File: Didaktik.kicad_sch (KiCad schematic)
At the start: 102 parts, among them J1 Conn_01x04_MountingPin, SW1 SW_Push, SW10 SW_Push_45deg, SW11 SW_Push_45deg, SW12 SW_Push_45deg, SW13 SW_Push_45deg, SW14 SW_Push_45deg, SW15 SW_Push_45deg, SW16 SW_Push_45deg, SW17 SW_Push_45deg, SW18 SW_Push_45deg, SW19 SW_Push_45deg, SW2 SW_Push_45deg, SW20 SW_Push_45deg, SW21 SW_Push_45deg, SW22 SW_Push_45deg, SW23 SW_Push_45deg, SW24 SW_Push_45deg, SW25 SW_Push_45deg, SW26 SW_Push_45deg, SW27 SW_Push_45deg, SW28 SW_Push_45deg, SW29 SW_Push_45deg, SW3 SW_Push_45deg, SW30 SW_Push_45deg, SW31 SW_Push_45deg, SW32 SW_Push_45deg, SW33 SW_Push_45deg, SW34 SW_Push_45deg, SW35 SW_Push_45deg, SW36 SW_Push_45deg, SW37 SW_Push_45deg, SW38 SW_Push_45deg, SW39 SW_Push_45deg, SW4 SW_Push_45deg, SW40 SW_Push_45deg, SW41 SW_Push_45deg, SW5 SW_Push_45deg, SW6 SW_Push_45deg, SW7 SW_Push_45deg, SW8 SW_Push_45deg, SW9 SW_Push_45deg, U1 ATmega32U4-M, Y1 Crystal_GND24_Small

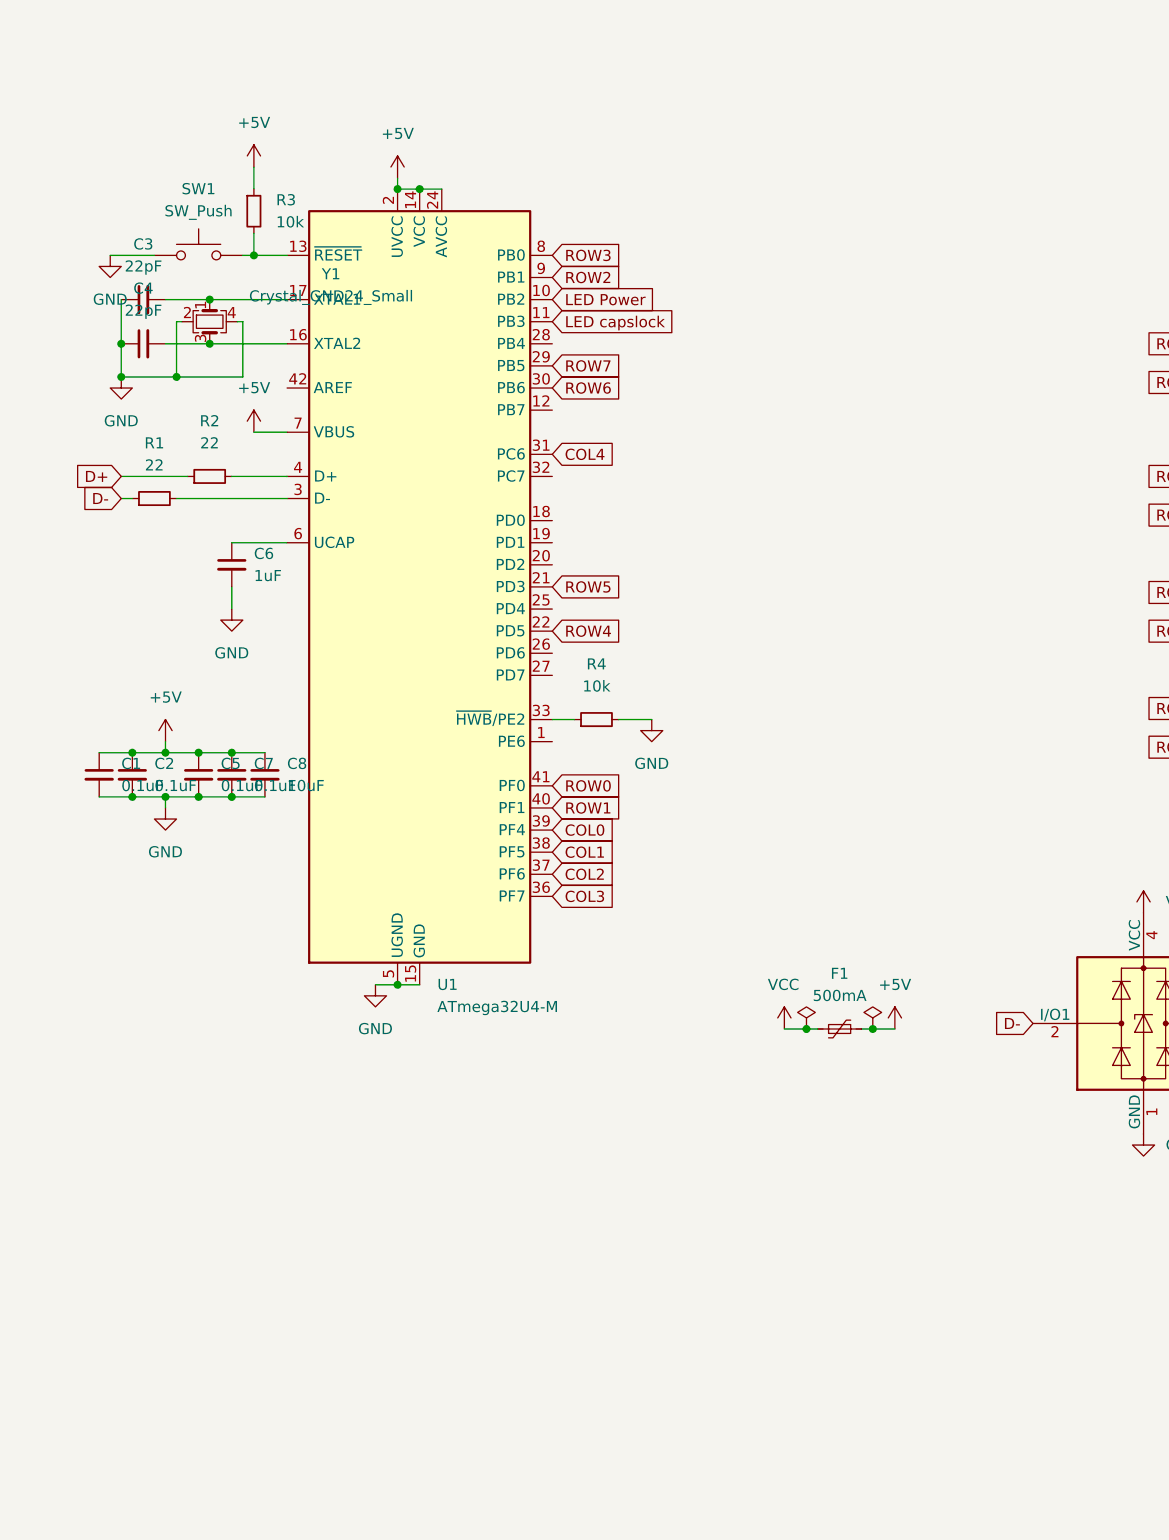
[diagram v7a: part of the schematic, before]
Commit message: added ISP to 40, added ISP schematics to 45
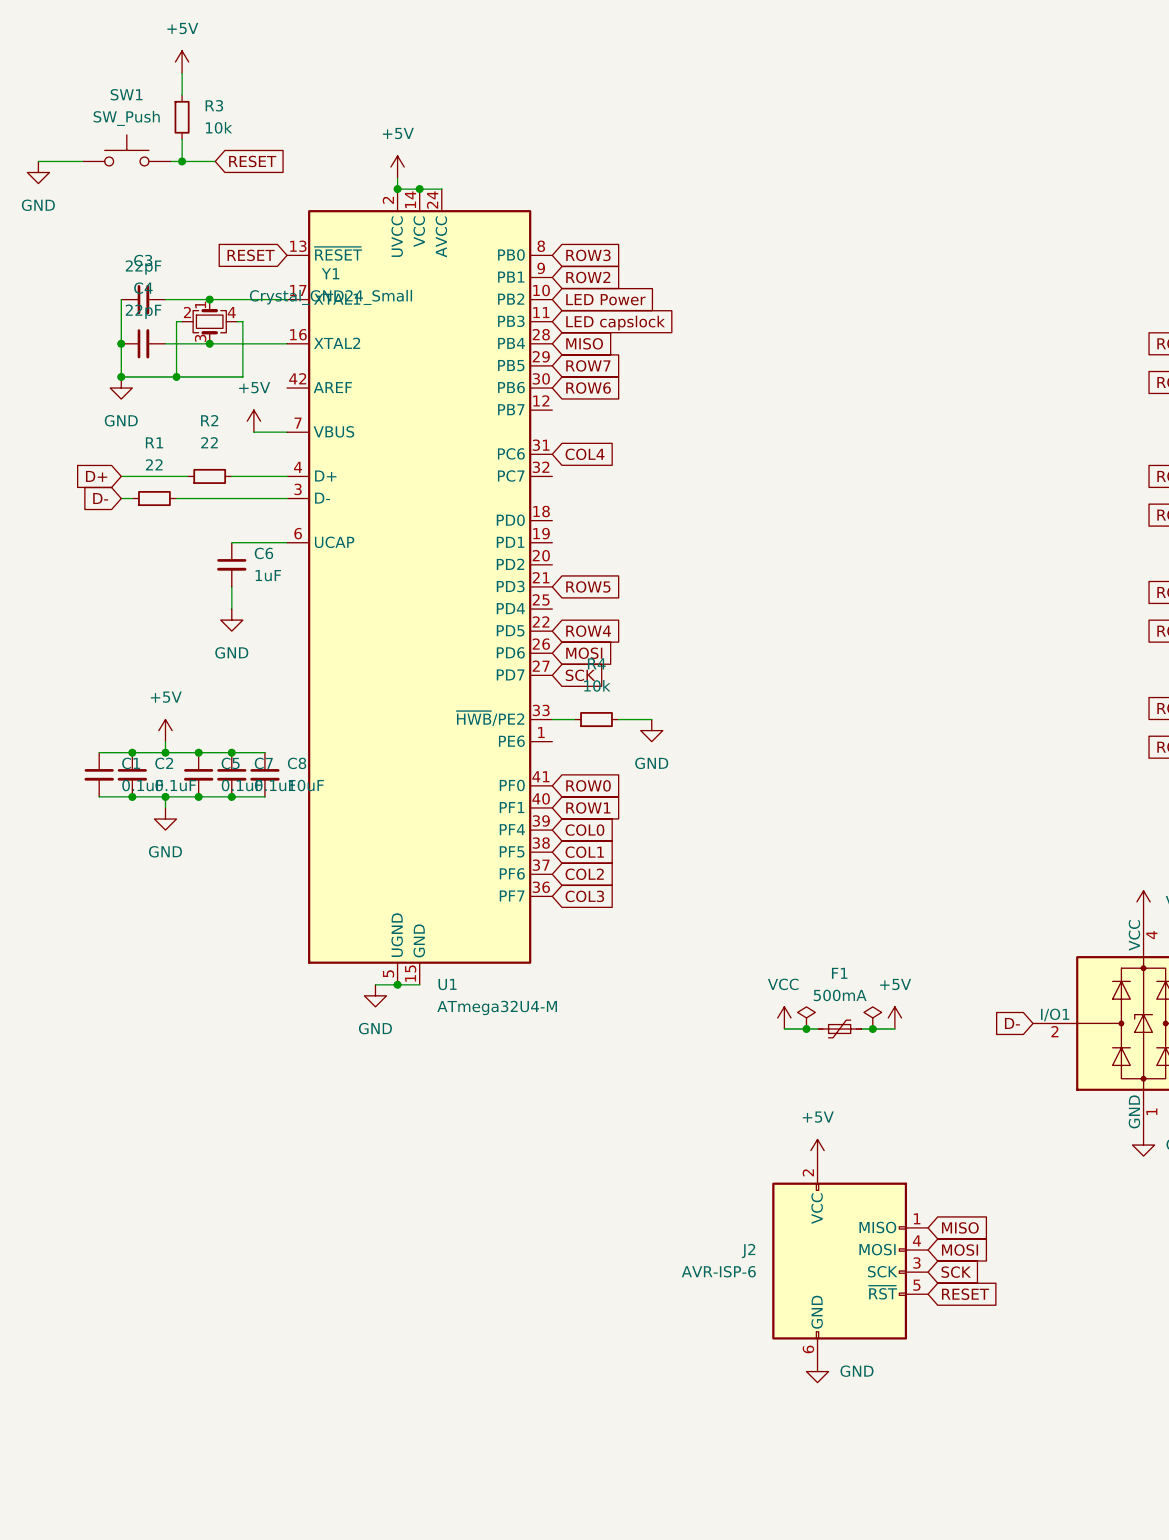
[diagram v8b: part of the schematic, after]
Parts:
- added J2: AVR-ISP-6, random-keyboard-parts:Reset_Pretty-Mask, symbol Connector:AVR-ISP-6
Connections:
- net +5V: now also J2.2 (VCC)
- net GND: now also J2.6 (GND)
- net RESET: now reaches R3.2, SW1.2, U1.13 (~{RESET})
- net RESET: now also J2.5 (~{RST})
- net MOSI: now reaches U1.26 (PD6)
- net MOSI: now also J2.4 (MOSI)
- net SCK: now reaches U1.27 (PD7)
- net SCK: now also J2.3 (SCK)
- net MISO: now reaches U1.28 (PB4)
- net MISO: now also J2.1 (MISO)
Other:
- moved on the sheet: R3, SW1
